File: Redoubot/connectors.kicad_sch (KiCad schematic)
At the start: 6 parts, among them J1 Connecteur batterie, J2 Moteur 1, J3 Moteur 2, J4 TOF, J5 MPU-6050, J6 ADA3595

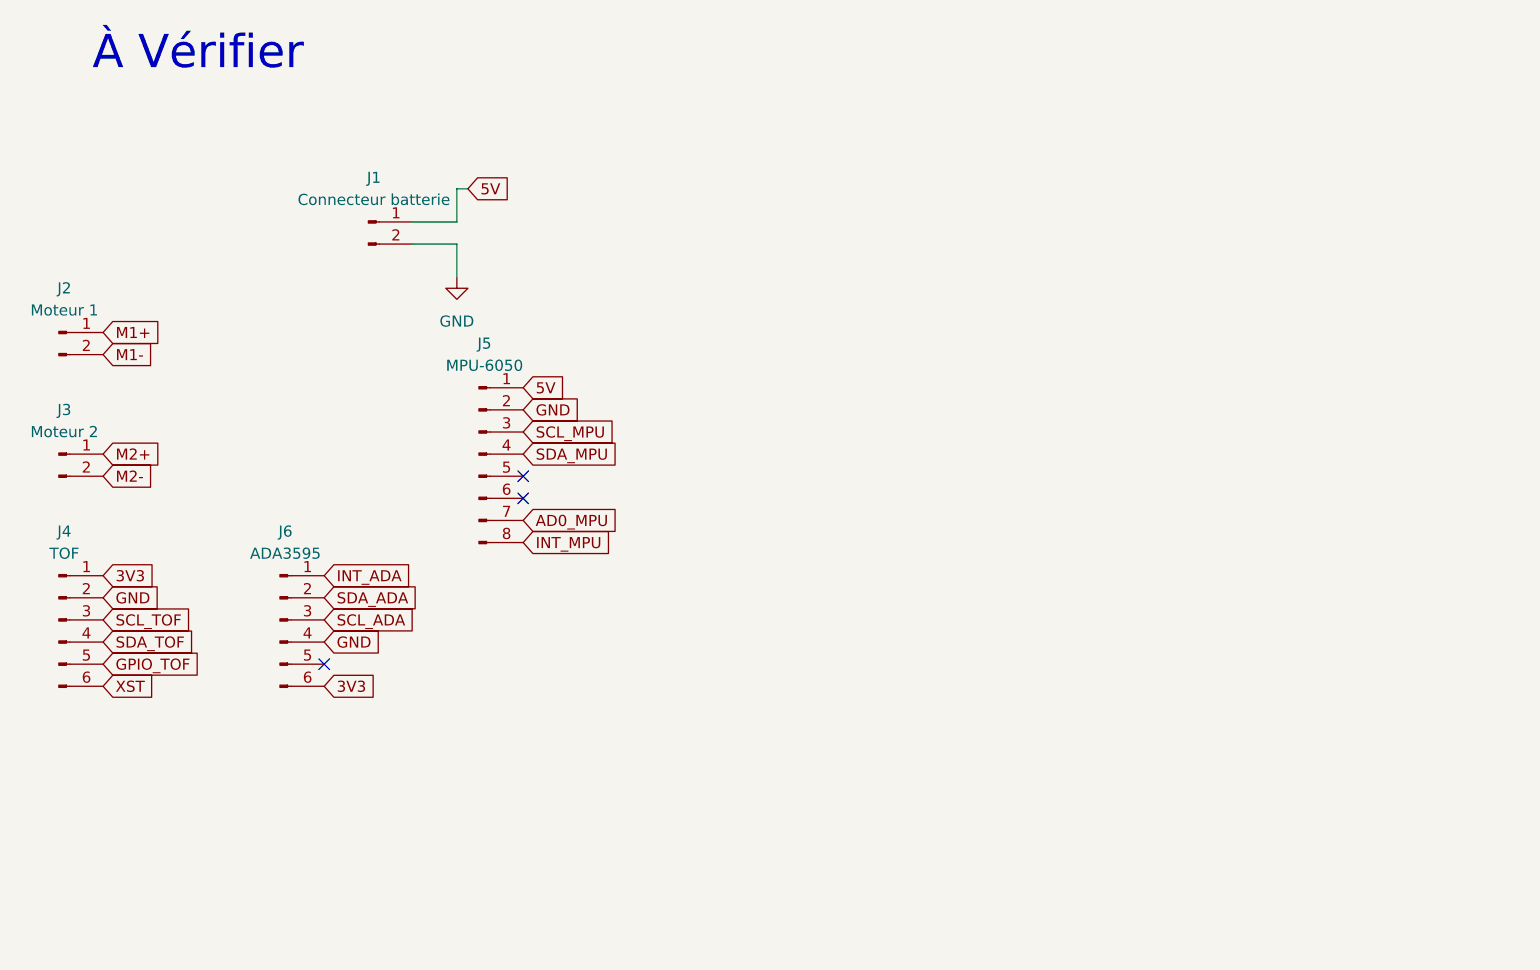
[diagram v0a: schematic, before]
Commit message: chore: renaming of hierchical sheet power to power_management to better match the use, creation of drivers and sensors HS to have clear sheets
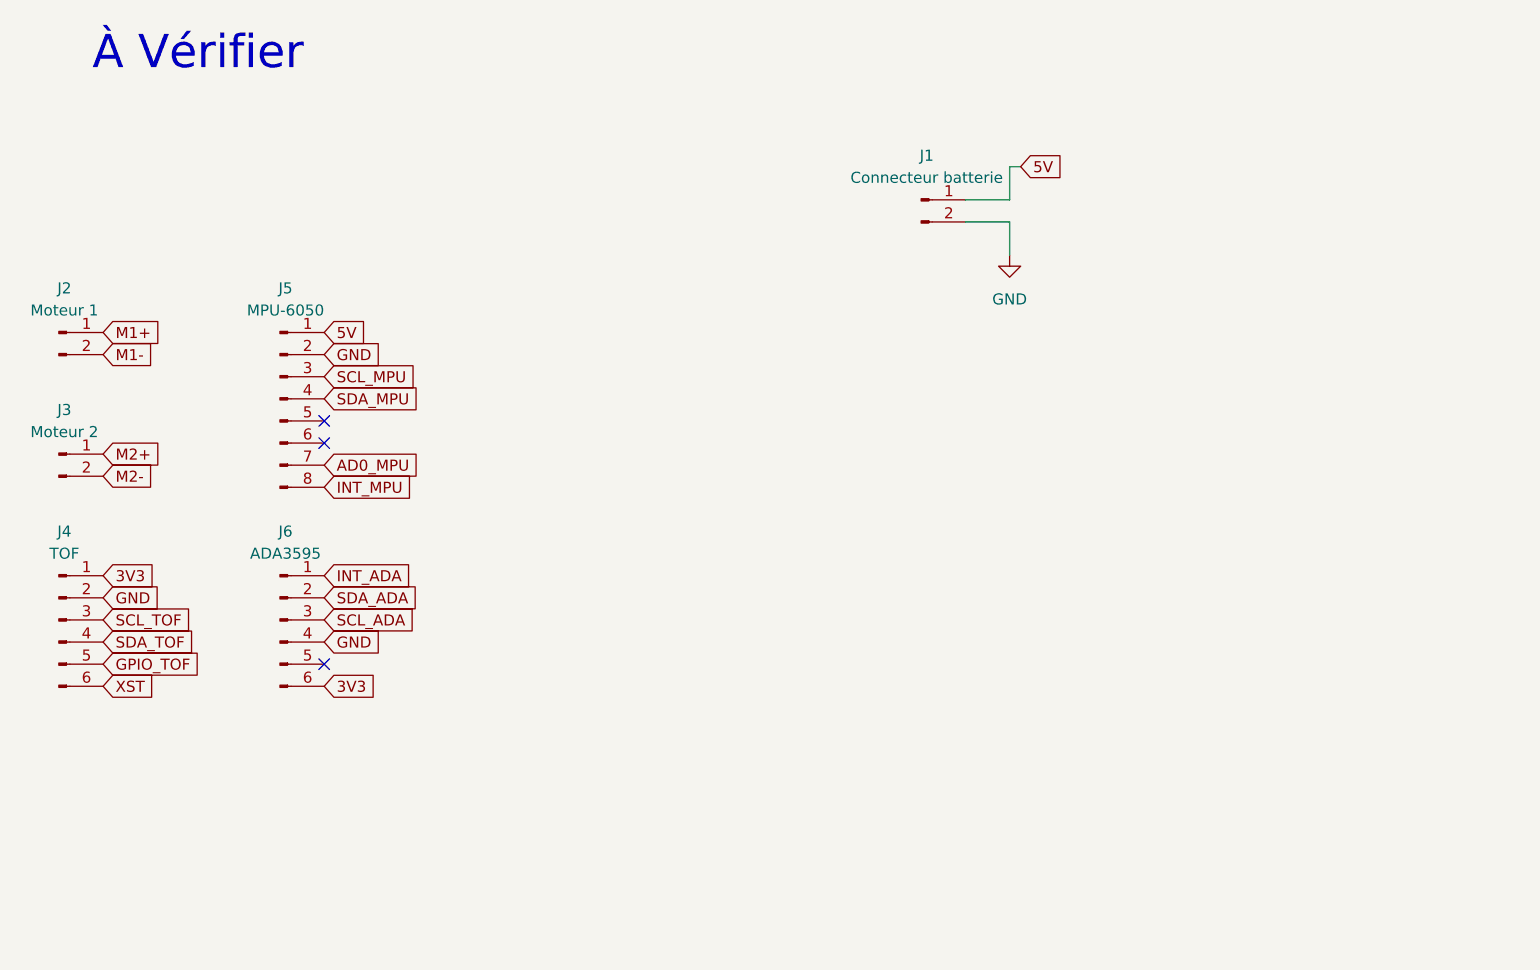
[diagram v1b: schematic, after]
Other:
- moved on the sheet: J1, J5
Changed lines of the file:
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@@
 	)
 	(no_connect
-		(at 97.79 80.01)
+		(at 74.93 73.66)
 	)
 	(no_connect
-		(at 97.79 77.47)
+		(at 74.93 71.12)
 	)
 	(wire
 		(pts
-			(xy 90.17 48.26) (xy 85.09 48.26)
+			(xy 153.67 45.72) (xy 148.59 45.72)
 		)
 		(stroke
@@
 	(wire
 		(pts
-			(xy 90.17 44.45) (xy 90.17 48.26)
+			(xy 153.67 41.91) (xy 153.67 45.72)
 		)
 		(stroke
@@
 	(wire
 		(pts
-			(xy 90.17 50.8) (xy 90.17 54.61)
+			(xy 153.67 48.26) (xy 153.67 52.07)
 		)
 		(stroke
@@
 	(wire
 		(pts
-			(xy 85.09 50.8) (xy 90.17 50.8)
+			(xy 148.59 48.26) (xy 153.67 48.26)
 		)
 		(stroke
@@
 	(wire
 		(pts
-			(xy 91.44 44.45) (xy 90.17 44.45)
+			(xy 154.94 41.91) (xy 153.67 41.91)
 		)
 		(stroke
@@
 	(global_label "SCL_MPU"
 		(shape input)
-		(at 97.79 72.39 0)
-		(fields_autoplaced yes)
-		(effects
-			(font
-				(size 1.27 1.27)
-			)
-			(justify left)
-		)
-		(property "Intersheetrefs" "${INTERSHEET_REFS}"
-			(at 109.3023 72.39 0)
+		(at 74.93 66.04 0)
+		(fields_autoplaced yes)
+		(effects
+			(font
+				(size 1.27 1.27)
+			)
+			(justify left)
+		)
+		(property "Intersheetrefs" "${INTERSHEET_REFS}"
+			(at 86.4423 66.04 0)
 			(hide yes)
 			(show_name no)
@@
 	(global_label "GND"
 		(shape input)
-		(at 97.79 69.85 0)
-		(fields_autoplaced yes)
-		(effects
-			(font
-				(size 1.27 1.27)
-			)
-			(justify left)
-		)
-		(property "Intersheetrefs" "${INTERSHEET_REFS}"
-			(at 104.6457 69.85 0)
+		(at 74.93 63.5 0)
+		(fields_autoplaced yes)
+		(effects
+			(font
+				(size 1.27 1.27)
+			)
+			(justify left)
+		)
+		(property "Intersheetrefs" "${INTERSHEET_REFS}"
+			(at 81.7857 63.5 0)
 			(hide yes)
 			(show_name no)
@@
 	(global_label "5V"
 		(shape input)
-		(at 91.44 44.45 0)
-		(fields_autoplaced yes)
-		(effects
-			(font
-				(size 1.27 1.27)
-			)
-			(justify left)
-		)
-		(property "Intersheetrefs" "${INTERSHEET_REFS}"
-			(at 96.7233 44.45 0)
+		(at 154.94 41.91 0)
+		(fields_autoplaced yes)
+		(effects
+			(font
+				(size 1.27 1.27)
+			)
+			(justify left)
+		)
+		(property "Intersheetrefs" "${INTERSHEET_REFS}"
+			(at 160.2233 41.91 0)
 			(hide yes)
 			(show_name no)
@@
 	(global_label "SDA_MPU"
 		(shape input)
-		(at 97.79 74.93 0)
-		(fields_autoplaced yes)
-		(effects
-			(font
-				(size 1.27 1.27)
-			)
-			(justify left)
-		)
-		(property "Intersheetrefs" "${INTERSHEET_REFS}"
-			(at 109.3628 74.93 0)
+		(at 74.93 68.58 0)
+		(fields_autoplaced yes)
+		(effects
+			(font
+				(size 1.27 1.27)
+			)
+			(justify left)
+		)
+		(property "Intersheetrefs" "${INTERSHEET_REFS}"
+			(at 86.5028 68.58 0)
 			(hide yes)
 			(show_name no)
@@
 	(global_label "AD0_MPU"
 		(shape input)
-		(at 97.79 82.55 0)
-		(fields_autoplaced yes)
-		(effects
-			(font
-				(size 1.27 1.27)
-			)
-			(justify left)
-		)
-		(property "Intersheetrefs" "${INTERSHEET_REFS}"
-			(at 109.3628 82.55 0)
+		(at 74.93 76.2 0)
+		(fields_autoplaced yes)
+		(effects
+			(font
+				(size 1.27 1.27)
+			)
+			(justify left)
+		)
+		(property "Intersheetrefs" "${INTERSHEET_REFS}"
+			(at 86.5028 76.2 0)
 			(hide yes)
 			(show_name no)
@@
 	(global_label "INT_MPU"
 		(shape input)
-		(at 97.79 85.09 0)
-		(fields_autoplaced yes)
-		(effects
-			(font
-				(size 1.27 1.27)
-			)
-			(justify left)
-		)
-		(property "Intersheetrefs" "${INTERSHEET_REFS}"
-			(at 108.6976 85.09 0)
+		(at 74.93 78.74 0)
+		(fields_autoplaced yes)
+		(effects
+			(font
+				(size 1.27 1.27)
+			)
+			(justify left)
+		)
+		(property "Intersheetrefs" "${INTERSHEET_REFS}"
+			(at 85.8376 78.74 0)
 			(hide yes)
 			(show_name no)
@@
 	(global_label "5V"
 		(shape input)
-		(at 97.79 67.31 0)
-		(fields_autoplaced yes)
-		(effects
-			(font
-				(size 1.27 1.27)
-			)
-			(justify left)
-		)
-		(property "Intersheetrefs" "${INTERSHEET_REFS}"
-			(at 103.0733 67.31 0)
+		(at 74.93 60.96 0)
+		(fields_autoplaced yes)
+		(effects
+			(font
+				(size 1.27 1.27)
+			)
+			(justify left)
+		)
+		(property "Intersheetrefs" "${INTERSHEET_REFS}"
+			(at 80.2133 60.96 0)
 			(hide yes)
 			(show_name no)
@@
 	(symbol
 		(lib_id "Connector:Conn_01x08_Pin")
-		(at 92.71 74.93 0)
+		(at 69.85 68.58 0)
 		(unit 1)
 		(body_style 1)
@@
 		(fields_autoplaced yes)
 		(property "Reference" "J5"
-			(at 93.345 62.23 0)
+			(at 70.485 55.88 0)
 			(show_name no)
 			(do_not_autoplace no)
@@
 		)
 		(property "Value" "MPU-6050"
-			(at 93.345 64.77 0)
+			(at 70.485 58.42 0)
 			(show_name no)
 			(do_not_autoplace no)
@@
 		)
 		(property "Footprint" ""
-			(at 92.71 74.93 0)
+			(at 69.85 68.58 0)
 			(hide yes)
 			(show_name no)
@@
 		)
 		(property "Datasheet" ""
-			(at 92.71 74.93 0)
+			(at 69.85 68.58 0)
 			(hide yes)
 			(show_name no)
@@
 		)
 		(property "Description" "Generic connector, single row, 01x08, script generated"
-			(at 92.71 74.93 0)
+			(at 69.85 68.58 0)
 			(hide yes)
 			(show_name no)
@@
 	(symbol
 		(lib_id "power:GND")
-		(at 90.17 54.61 0)
+		(at 153.67 52.07 0)
 		(unit 1)
 		(body_style 1)
@@
 		(fields_autoplaced yes)
 		(property "Reference" "#PWR01"
-			(at 90.17 60.96 0)
+			(at 153.67 58.42 0)
 			(hide yes)
 			(show_name no)
@@
 		)
 		(property "Value" "GND"
-			(at 90.17 59.69 0)
+			(at 153.67 57.15 0)
 			(show_name no)
 			(do_not_autoplace no)
@@
 		)
 		(property "Footprint" ""
-			(at 90.17 54.61 0)
+			(at 153.67 52.07 0)
 			(hide yes)
 			(show_name no)
@@
 		)
 		(property "Datasheet" ""
-			(at 90.17 54.61 0)
+			(at 153.67 52.07 0)
 			(hide yes)
 			(show_name no)
@@
 		)
 		(property "Description" "Power symbol creates a global label with name \"GND\" , ground"
-			(at 90.17 54.61 0)
+			(at 153.67 52.07 0)
 			(hide yes)
 			(show_name no)
@@
 	(symbol
 		(lib_id "Connector:Conn_01x02_Pin")
-		(at 80.01 48.26 0)
+		(at 143.51 45.72 0)
 		(unit 1)
 		(body_style 1)
@@
 		(fields_autoplaced yes)
 		(property "Reference" "J1"
-			(at 80.645 43.18 0)
+			(at 144.145 40.64 0)
 			(show_name no)
 			(do_not_autoplace no)
@@
 		)
 		(property "Value" "Connecteur batterie"
-			(at 80.645 45.72 0)
+			(at 144.145 43.18 0)
 			(show_name no)
 			(do_not_autoplace no)
@@
 		)
 		(property "Footprint" ""
-			(at 80.01 48.26 0)
+			(at 143.51 45.72 0)
 			(hide yes)
 			(show_name no)
@@
 		)
 		(property "Datasheet" ""
-			(at 80.01 48.26 0)
+			(at 143.51 45.72 0)
 			(hide yes)
 			(show_name no)
@@
 		)
 		(property "Description" "Generic connector, single row, 01x02, script generated"
-			(at 80.01 48.26 0)
-			(hide yes)
-			(show_name no)
+			(at 143.51 45.72 0)
+			(hide yes)
+			(show_name no)

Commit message: feat: added all remaining connectors & finished putting values on components
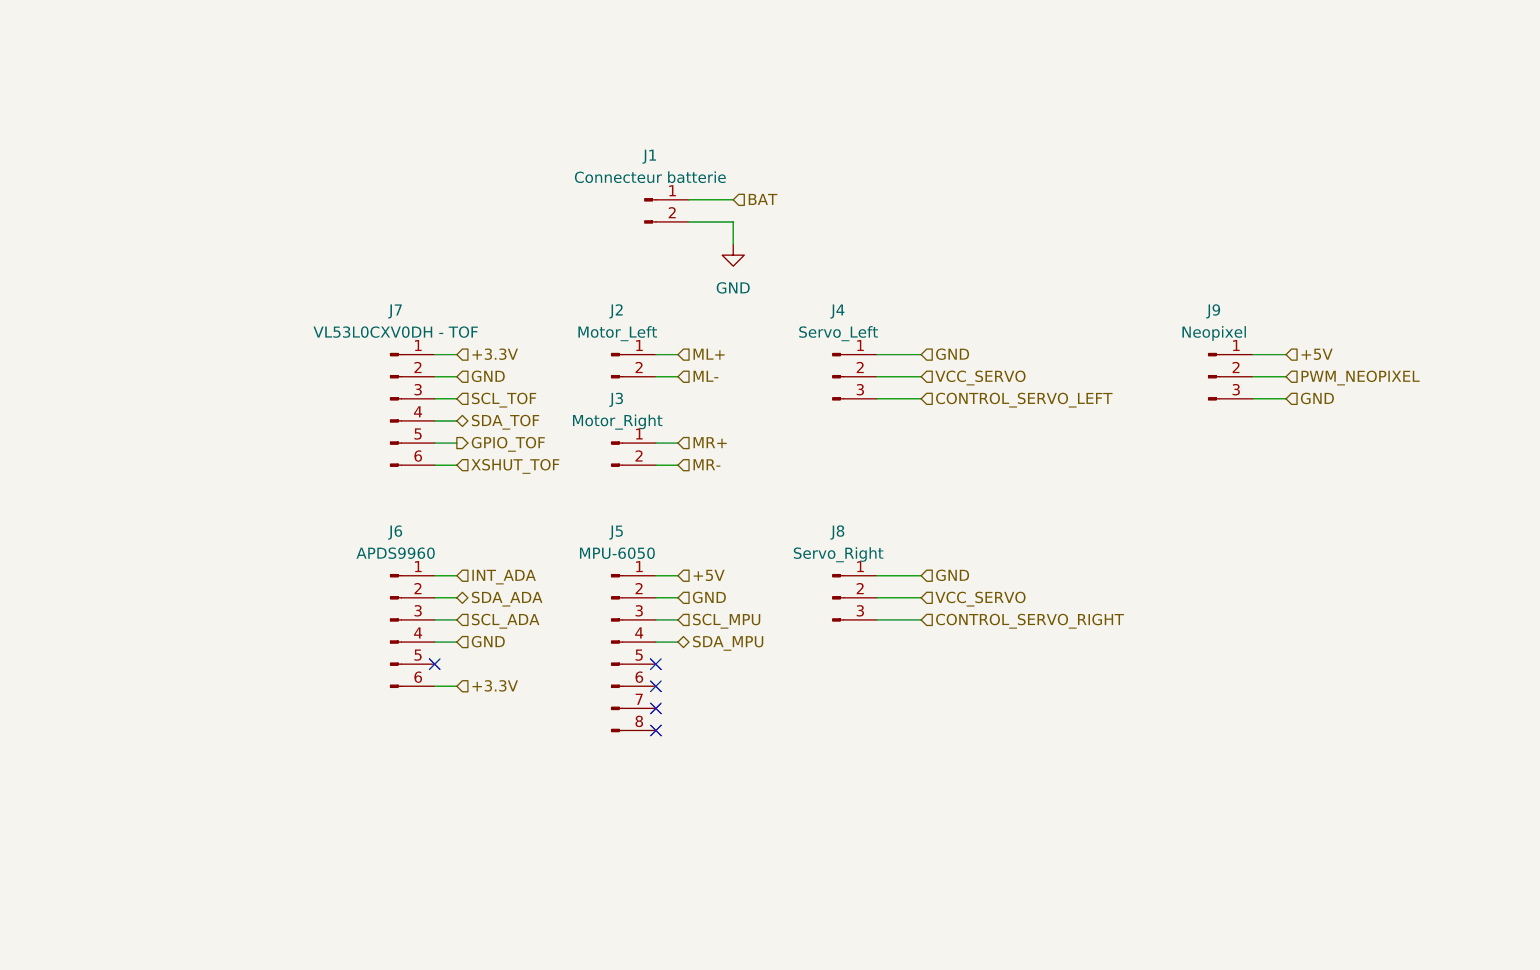
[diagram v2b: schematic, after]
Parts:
- removed J4: TOF, symbol Connector:Conn_01x06_Pin
- added J4: Servo_Left, Package_BGA:BGA-256_17.0x17.0mm_Layout16x16_P1.0mm_Ball0.5mm_Pad0.4mm_NSMD, symbol Connector:Conn_01x03_Pin
- added J7: VL53L0CXV0DH - TOF, Package_BGA:BGA-256_17.0x17.0mm_Layout16x16_P1.0mm_Ball0.5mm_Pad0.4mm_NSMD, symbol Connector:Conn_01x06_Pin
- added J8: Servo_Right, symbol Connector:Conn_01x03_Pin
- added J9: Neopixel, symbol Connector:Conn_01x03_Pin
- J2: value Moteur 1 -> Motor_Left
- J3: value Moteur 2 -> Motor_Right
- J6: value ADA3595 -> APDS9960
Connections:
- net GND: now also J4.1 (Pin_1), J7.2 (Pin_2), J8.1 (Pin_1), J9.3 (Pin_3)
- net GPIO_TOF: now also J7.5 (Pin_5)
- net SCL_TOF: now also J7.3 (Pin_3)
- net SDA_TOF: now also J7.4 (Pin_4)
- net 3V3 renamed +3.3V
- net +3.3V: now also J7.1 (Pin_1)
- net 5V renamed +5V
- net +5V: now also J9.1 (Pin_1); no longer J1.1 (Pin_1)
- net AD0_MPU: no longer names the net of J5.7 (Pin_7)
- net INT_MPU: no longer names the net of J5.8 (Pin_8)
- net M1+ renamed ML+
- net M1- renamed ML-
- net M2+ renamed MR+
- net M2- renamed MR-
- new net BAT: J1.1 (Pin_1)
- new net CONTROL_SERVO_LEFT: J4.3 (Pin_3)
- new net CONTROL_SERVO_RIGHT: J8.3 (Pin_3)
- new net PWM_NEOPIXEL: J9.2 (Pin_2)
- new net VCC_SERVO: J4.2 (Pin_2), J8.2 (Pin_2)
- new net XSHUT_TOF: J7.6 (Pin_6)
- no-connect marks 3 -> 5
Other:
- note removed: "À Vérifier"
- moved on the sheet: J1, J2, J3, J5, J6

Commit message: chore: wired everything possible atm, wrote down every missing links, waiting for .ioc to continue
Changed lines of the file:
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@@
 	)
 	(hierarchical_label "BAT"
-		(shape input)
+		(shape output)
 		(at 121.92 45.72 0)
 		(effects

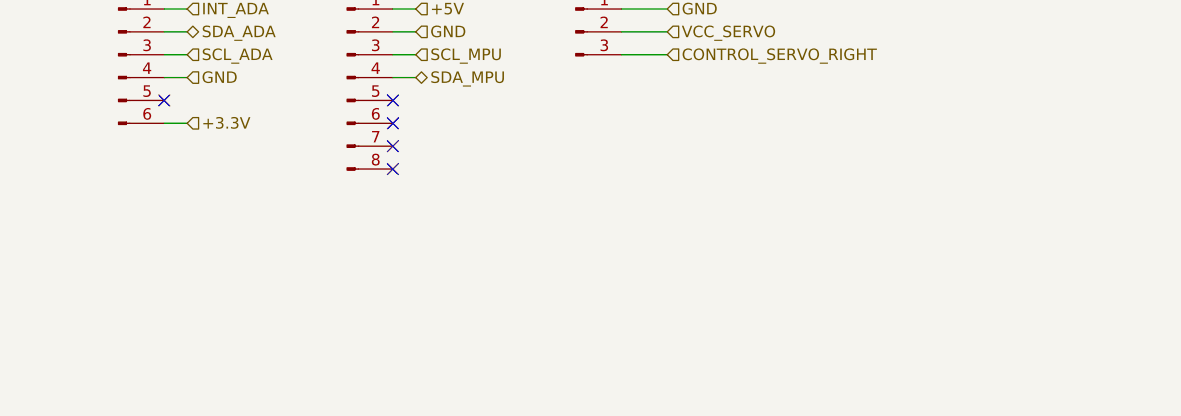
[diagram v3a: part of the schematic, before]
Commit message: feat: added DFPlayer Mini and HM10 connectors
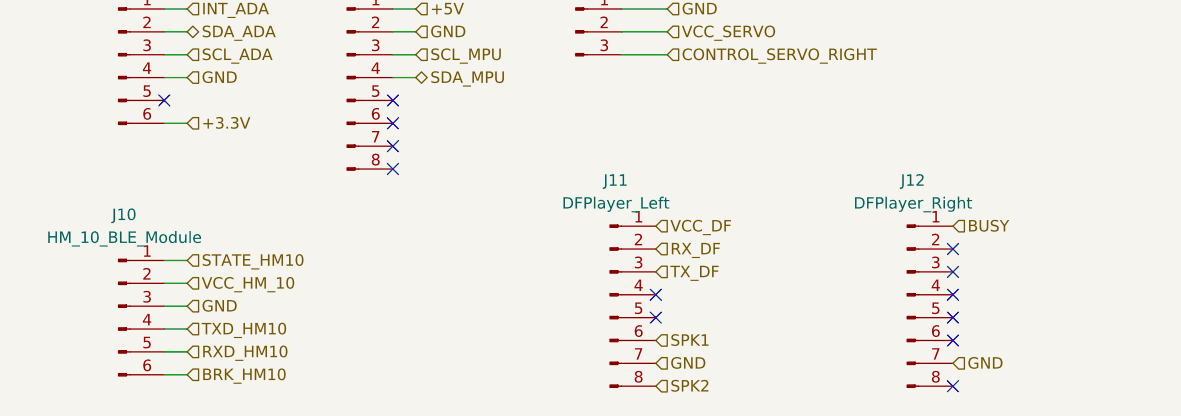
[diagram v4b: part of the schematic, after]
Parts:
- added J10: HM_10_BLE_Module, symbol Connector:Conn_01x06_Pin
- added J11: DFPlayer_Left, symbol Connector:Conn_01x08_Pin
- added J12: DFPlayer_Right, symbol Connector:Conn_01x08_Pin
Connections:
- net GND: now also J10.3 (Pin_3), J11.7 (Pin_7), J12.7 (Pin_7)
- new net BRK_HM10: J10.6 (Pin_6)
- new net BUSY: J12.1 (Pin_1)
- new net RXD_HM10: J10.5 (Pin_5)
- new net RX_DF: J11.2 (Pin_2)
- new net SPK1: J11.6 (Pin_6)
- new net SPK2: J11.8 (Pin_8)
- new net STATE_HM10: J10.1 (Pin_1)
- new net TXD_HM10: J10.4 (Pin_4)
- new net TX_DF: J11.3 (Pin_3)
- new net VCC_DF: J11.1 (Pin_1)
- new net VCC_HM_10: J10.2 (Pin_2)
- no-connect marks 5 -> 13

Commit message: simply added the JLCPCB Part # as an LCSC field in the component descriptions
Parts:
- J5: LCSC (none) -> C24112
- J7: LCSC (none) -> C91199
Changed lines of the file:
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@@
+			)
+		)
+		(property "LCSC" "C24112"
+			(at 107.95 96.52 0)
+			(hide yes)
+			(show_name no)
+			(do_not_autoplace no)
+			(effects
+				(font
+					(size 1.27 1.27)
+				)
 			)
 		)
@@
 			(at 82.55 68.58 0)
 			(hide yes)
+			(show_name no)
+			(do_not_autoplace no)
+			(effects
+				(font
+					(size 1.27 1.27)
+				)
+			)
+		)
+		(property "LCSC" "C91199"
+			(at 82.55 68.58 0)
+			(hide yes)
